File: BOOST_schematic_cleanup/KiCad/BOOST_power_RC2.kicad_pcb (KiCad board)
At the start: 8 copper layers, 74 x 86 mm, 135 parts, among them J1 Conn_01x01_Pin, J10 Conn_02x15_2.54mm, J2 Conn_01x01_Pin, J3 Conn_01x01_Pin, J4 Conn_01x01_Pin, J5 Conn_01x01_Pin, J6 Conn_01x01_Pin, J7 Conn_01x01_Pin, J8 Conn_01x01_Pin, M1 HYG180N10, M10 HYG180N10, M2 HYG180N10, M3 HYG180N10, M4 HYG180N10, M5 HYG180N10, M6 HYG180N10, M7 HYG180N10, M8 HYG180N10, M9 HYG180N10, U1 L78L05_SOT89, U10 UCC21520DW, U11 MCP6241, U12 MCP6241, U15 UCC21520DW, U16 LM2940_12, U17 L78L05_SOT89, U19 UCC21520DW, U25 INA241A4xD, U6 MCP6241, U8 UCC21520DW

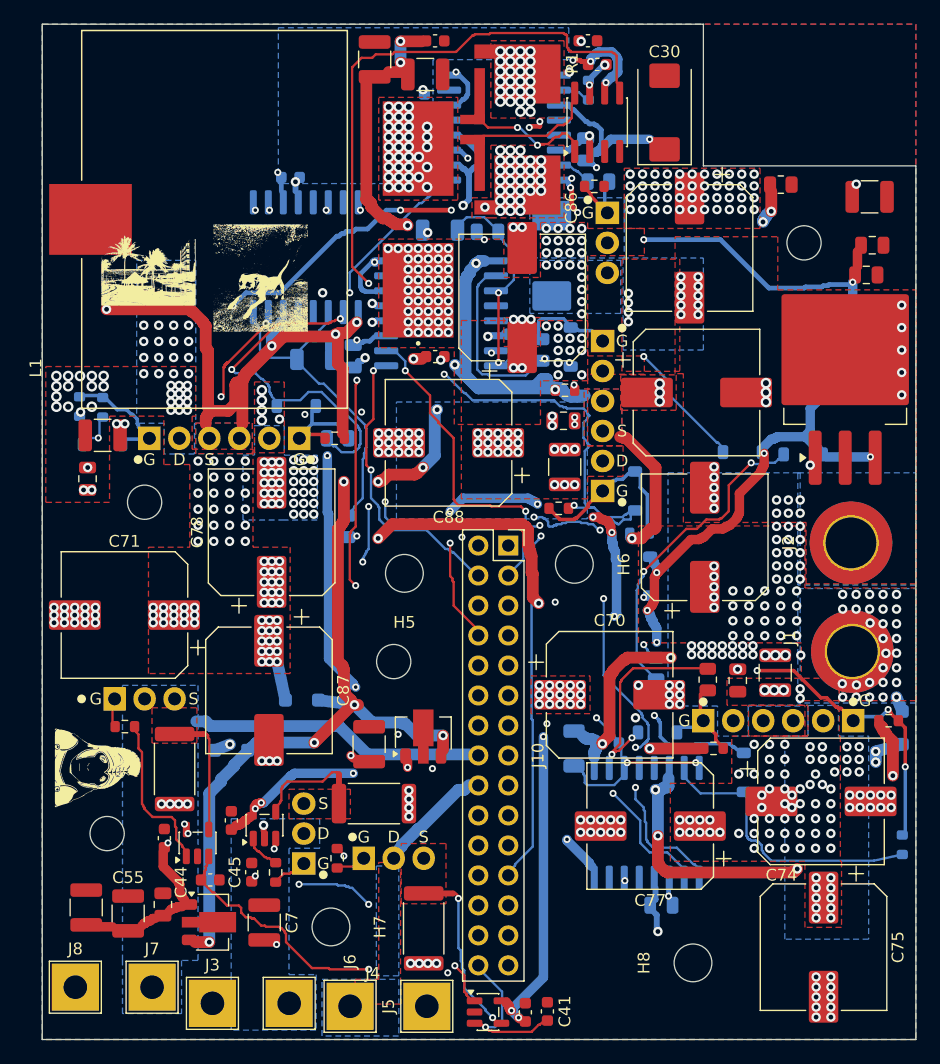
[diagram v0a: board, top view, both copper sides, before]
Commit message: changed power board to 6 layers
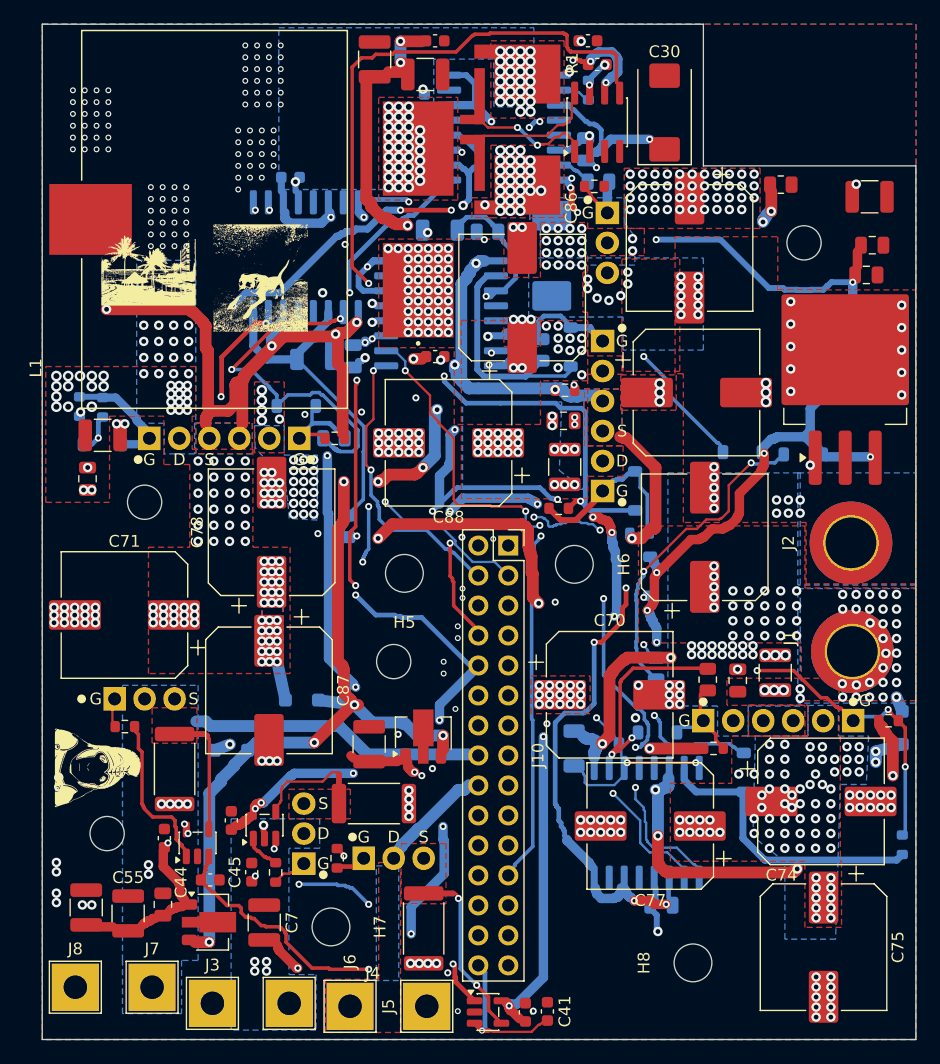
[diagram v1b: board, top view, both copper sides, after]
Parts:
- U11, U12, U6: value MCP6241 -> TLV9001
- U16: value LM2940_12 -> MC7812
- moved R70 0.31 mm to (54.7, 65.1)
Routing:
- net 5V: track 15.9 -> 205.5 mm, vias 13 -> 25
- net m2_source: track 53.7 -> 48.3 mm
- net Net-(U10-VDDA): track 23.1 -> 28.3 mm
- net GATE_M3: track 6.35 -> 10.3 mm
- net Net-(D11--): track 36.3 -> 32.7 mm
- net Net-(U15-VDDA): track 15.0 -> 18.2 mm
- net GATE_M2: track 10.8 -> 13.6 mm
- net M1_ON: track 48.7 -> 46.1 mm
- net Net-(D13--): track 22.8 -> 24.9 mm
- net Net-(D14--): track 23.0 -> 24.7 mm
- net 12V: track 127.8 -> 129.4 mm
- net GATE_M1: track 2.53 -> 4.04 mm
- net Net-(D8--): track 29.0 -> 30.4 mm
- net Net-(D2--): track 18.5 -> 19.4 mm, vias 2 -> 0
- net GATE_M7: track 8.61 -> 9.19 mm
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- added copper zone on In4.Cu, net GND
- added copper zone on In3.Cu, net LX
- added copper zone on In4.Cu, net LX
- added copper zone on In1.Cu, net Vin
- added copper zone on In4.Cu, net Vin
- added copper zone on In4.Cu, net Vout_1
- added copper zone on In1.Cu, net Vout_2
- added copper zone on In4.Cu, net Vout_2
- added copper zone on In4.Cu, net Vout_3
- added copper zone on In4.Cu, net m2_source
- added copper zone on In4.Cu, net m3_source
- added copper zone on In4.Cu, net m4_source
- added copper zone on In1.Cu, net rsense_lo
- added copper zone on In4.Cu, net rsense_lo
- removed copper zone on In4.Cu, net 5V
- removed copper zone on In5.Cu, net GND
- removed copper zone on In6.Cu, net GND
- removed copper zone on In5.Cu, net Vin
- removed copper zone on In5.Cu, net Vout_1
- removed copper zone on In5.Cu, net Vout_2
- removed copper zone on In5.Cu, net Vout_3
- removed copper zone on In5.Cu, net m2_source
- removed copper zone on In5.Cu, net m3_source
- removed copper zone on In5.Cu, net m4_source
- removed copper zone on In5.Cu, net rsense_lo
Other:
- copper layers 8 -> 6
